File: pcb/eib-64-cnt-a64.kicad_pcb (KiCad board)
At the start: 4 copper layers, 20 x 53.6 mm, 5 parts, among them J1 FOLC-110-01-S-Q, J2 FOLC-110-01-S-Q, J3 DF40C(2.0)-70DS-0.4V(51), J4 Conn_01x07_Male

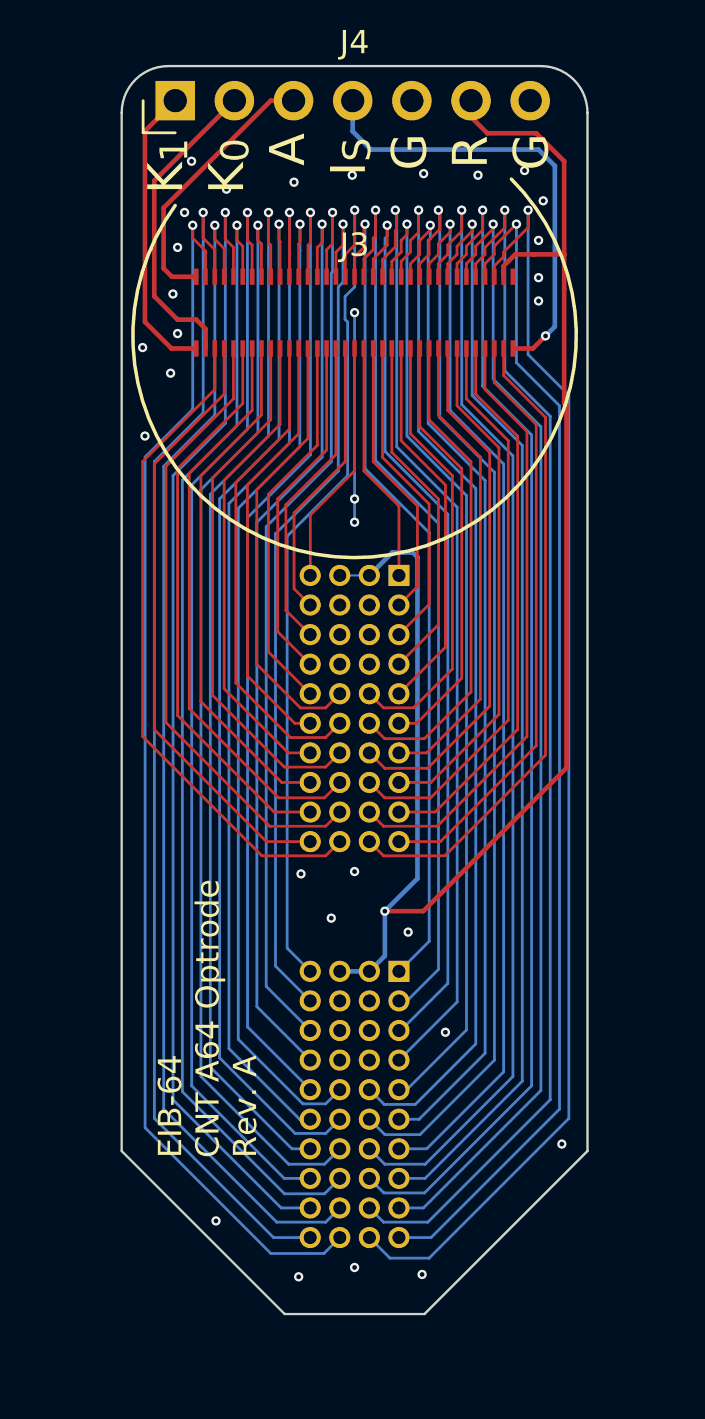
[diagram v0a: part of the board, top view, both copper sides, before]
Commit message: Revision A
- Set to JLC for production
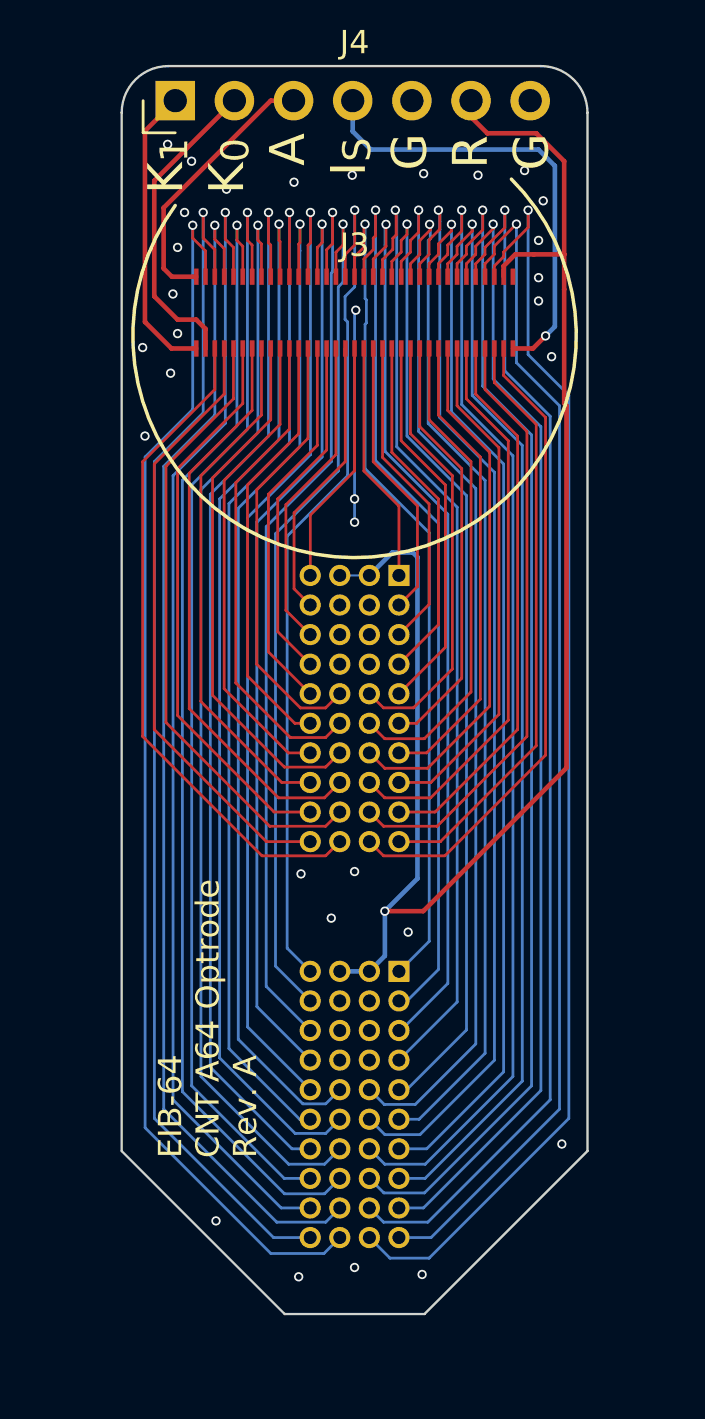
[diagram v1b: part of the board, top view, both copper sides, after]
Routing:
- net GND: track 26.7 -> 26.9 mm, vias 31 -> 32

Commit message: Revision A
- This was fabricated and tested.
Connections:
- J1 pad A1: /Elec15 -> /Elec31
- J1 pad A10: /Elec1 -> /Elec3
- J1 pad A2: /Elec14 -> /Elec29
- J1 pad A3: /Elec13 -> /Elec27
- J1 pad A4: /Elec12 -> /Elec25
- J1 pad A5: /Elec11 -> /Elec23
- J1 pad A6: /Elec9 -> /Elec19
- J1 pad A7: /Elec7 -> /Elec15
- J1 pad A8: /Elec5 -> /Elec11
- J1 pad A9: /Elec3 -> /Elec7
- J1 pad B10: /Elec0 -> /Elec1
- J1 pad B5: /Elec10 -> /Elec21
- J1 pad B6: /Elec8 -> /Elec17
- J1 pad B7: /Elec6 -> /Elec13
- J1 pad B8: /Elec4 -> /Elec9
- J1 pad B9: /Elec2 -> /Elec5
- J1 pad C5: /Elec53 -> /Elec43
- J1 pad C6: /Elec55 -> /Elec47
- J1 pad C7: /Elec57 -> /Elec51
- J1 pad C8: /Elec59 -> /Elec55
- J1 pad C9: /Elec61 -> /Elec59
- J1 pad D1: /Elec48 -> /Elec33
- J1 pad D10: /Elec62 -> /Elec61
- J1 pad D2: /Elec49 -> /Elec35
- J1 pad D3: /Elec50 -> /Elec37
- J1 pad D4: /Elec51 -> /Elec39
- J1 pad D5: /Elec52 -> /Elec41
- J1 pad D6: /Elec54 -> /Elec45
- J1 pad D7: /Elec56 -> /Elec49
- J1 pad D8: /Elec58 -> /Elec53
- J1 pad D9: /Elec60 -> /Elec57
- J2 pad A1: /Elec31 -> /Elec30
- J2 pad A10: /Elec17 -> /Elec2
- J2 pad A2: /Elec30 -> /Elec28
- J2 pad A3: /Elec29 -> /Elec26
- J2 pad A4: /Elec28 -> /Elec24
- J2 pad A5: /Elec27 -> /Elec22
- J2 pad A6: /Elec25 -> /Elec18
- J2 pad A7: /Elec23 -> /Elec14
- J2 pad A8: /Elec21 -> /Elec10
- J2 pad A9: /Elec19 -> /Elec6
- J2 pad B10: /Elec16 -> /Elec0
- J2 pad B5: /Elec26 -> /Elec20
- J2 pad B6: /Elec24 -> /Elec16
- J2 pad B7: /Elec22 -> /Elec12
- J2 pad B8: /Elec20 -> /Elec8
- J2 pad B9: /Elec18 -> /Elec4
- J2 pad C10: /Elec47 -> /Elec62
- J2 pad C5: /Elec37 -> /Elec42
- J2 pad C6: /Elec39 -> /Elec46
- J2 pad C7: /Elec41 -> /Elec50
- J2 pad C8: /Elec43 -> /Elec54
- J2 pad C9: /Elec45 -> /Elec58
- J2 pad D10: /Elec46 -> /Elec60
- J2 pad D2: /Elec33 -> /Elec34
- J2 pad D3: /Elec34 -> /Elec36
- J2 pad D4: /Elec35 -> /Elec38
- J2 pad D5: /Elec36 -> /Elec40
- J2 pad D6: /Elec38 -> /Elec44
- J2 pad D7: /Elec40 -> /Elec48
- J2 pad D8: /Elec42 -> /Elec52
- J2 pad D9: /Elec44 -> /Elec56
- J3 pad 10: /Elec2 -> /Elec5
- J3 pad 11: /Elec20 -> /Elec8
- J3 pad 12: /Elec3 -> /Elec7
- J3 pad 13: /Elec21 -> /Elec10
- J3 pad 14: /Elec4 -> /Elec9
- J3 pad 15: /Elec22 -> /Elec12
- J3 pad 16: /Elec5 -> /Elec11
- J3 pad 17: /Elec23 -> /Elec14
- J3 pad 18: /Elec6 -> /Elec13
- J3 pad 19: /Elec24 -> /Elec16
- J3 pad 20: /Elec7 -> /Elec15
- J3 pad 21: /Elec25 -> /Elec18
- J3 pad 22: /Elec8 -> /Elec17
- J3 pad 23: /Elec26 -> /Elec20
- J3 pad 24: /Elec9 -> /Elec19
- J3 pad 25: /Elec27 -> /Elec22
- J3 pad 26: /Elec10 -> /Elec21
- J3 pad 27: /Elec28 -> /Elec24
- J3 pad 28: /Elec11 -> /Elec23
- J3 pad 29: /Elec29 -> /Elec26
- J3 pad 3: /Elec16 -> /Elec0
- J3 pad 30: /Elec12 -> /Elec25
- J3 pad 31: /Elec30 -> /Elec28
- J3 pad 32: /Elec13 -> /Elec27
- J3 pad 33: /Elec31 -> /Elec30
- J3 pad 34: /Elec14 -> /Elec29
- J3 pad 36: /Elec15 -> /Elec31
- J3 pad 37: /Elec33 -> /Elec34
- J3 pad 38: /Elec48 -> /Elec33
- J3 pad 39: /Elec34 -> /Elec36
- J3 pad 40: /Elec49 -> /Elec35
- J3 pad 41: /Elec35 -> /Elec38
- J3 pad 42: /Elec50 -> /Elec37
- J3 pad 43: /Elec36 -> /Elec40
- J3 pad 44: /Elec51 -> /Elec39
- J3 pad 45: /Elec37 -> /Elec42
- J3 pad 46: /Elec52 -> /Elec41
- J3 pad 47: /Elec38 -> /Elec44
- J3 pad 48: /Elec53 -> /Elec43
- J3 pad 49: /Elec39 -> /Elec46
- J3 pad 5: /Elec17 -> /Elec2
- J3 pad 50: /Elec54 -> /Elec45
- J3 pad 51: /Elec40 -> /Elec48
- J3 pad 52: /Elec55 -> /Elec47
- J3 pad 53: /Elec41 -> /Elec50
- J3 pad 54: /Elec56 -> /Elec49
- J3 pad 55: /Elec42 -> /Elec52
- J3 pad 56: /Elec57 -> /Elec51
- J3 pad 57: /Elec43 -> /Elec54
- J3 pad 58: /Elec58 -> /Elec53
- J3 pad 59: /Elec44 -> /Elec56
- J3 pad 6: /Elec0 -> /Elec1
- J3 pad 60: /Elec59 -> /Elec55
- J3 pad 61: /Elec45 -> /Elec58
- J3 pad 62: /Elec60 -> /Elec57
- J3 pad 63: /Elec46 -> /Elec60
- J3 pad 64: /Elec61 -> /Elec59
- J3 pad 65: /Elec47 -> /Elec62
- J3 pad 66: /Elec62 -> /Elec61
- J3 pad 7: /Elec18 -> /Elec4
- J3 pad 8: /Elec1 -> /Elec3
- J3 pad 9: /Elec19 -> /Elec6
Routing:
- net /Elec2: track 52.6 -> 25.4 mm, vias 1 -> 0
- net /Elec0: track 54.6 -> 27.8 mm, vias 1 -> 0
- net /Elec31: track 10.4 -> 36.3 mm, vias 0 -> 1
- net /Elec6: track 49.4 -> 23.7 mm, vias 1 -> 0
- net /Elec33: track 12.2 -> 37.4 mm, vias 0 -> 1
- net /Elec29: track 13.6 -> 38.7 mm, vias 0 -> 1
- net /Elec4: track 50.9 -> 26.0 mm, vias 1 -> 0
- net /Elec21: track 22.0 -> 45.9 mm, vias 0 -> 1
- net /Elec10: track 45.9 -> 22.0 mm, vias 1 -> 0
- net /Elec60: track 49.8 -> 26.3 mm, vias 1 -> 0
- net /Elec25: track 18.4 -> 41.8 mm, vias 0 -> 1
- net /Elec8: track 47.7 -> 24.3 mm, vias 1 -> 0
- net /Elec62: track 51.5 -> 28.8 mm, vias 1 -> 0
- net /Elec27: track 16.4 -> 39.1 mm, vias 0 -> 1
- net /Elec35: track 15.0 -> 37.6 mm, vias 0 -> 1
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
